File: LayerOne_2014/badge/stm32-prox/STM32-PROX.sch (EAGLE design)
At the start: 167 parts, among them IC10 74XX244-OCTAL-TRISTATE-BUFFERS, IC105 MCP1824T-250, IC106 MCP1824T-120, IC11 CD4066, IC13 PQ1X331M2ZP-3V3-LDO-SOT-23-5, IC14 AD8052, IC2 STM32F103RET6, IC3 PQ1X331M2ZP-3V3-LDO-SOT-23-5, IC4 HCU-INVERTER, IC5 TLV3502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

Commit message: 
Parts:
- added R7, R8: 27, resistor:R-US_R0805
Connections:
- new net N$1: IC2.PA11/UART1CTS/CNRX/TIM1CH4/USBD-, R7.2
- new net N$7: IC2.PA12/UART1RTS/CNTX/TIM1ETR/USBD+, R8.2
- net USB_D+: now also R8.1; no longer IC2.PA12/UART1RTS/CNTX/TIM1ETR/USBD+
- net USB_D-: now also R7.1; no longer IC2.PA11/UART1CTS/CNRX/TIM1CH4/USBD-
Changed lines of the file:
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@@
 <grid distance="0.1" unitdist="inch" unit="inch" style="lines" multiple="1" display="no" altdistance="0.01" altunitdist="inch" altunit="inch"/>
 <layers>
-<layer number="1" name="Top" color="4" fill="1" visible="yes" active="no"/>
-<layer number="2" name="Route2" color="1" fill="3" visible="yes" active="no"/>
-<layer number="3" name="Route3" color="4" fill="3" visible="yes" active="no"/>
-<layer number="4" name="Route4" color="1" fill="4" visible="yes" active="no"/>
-<layer number="5" name="Route5" color="4" fill="4" visible="yes" active="no"/>
-<layer number="6" name="Route6" color="1" fill="8" visible="yes" active="no"/>
-<layer number="7" name="Route7" color="4" fill="8" visible="yes" active="no"/>
-<layer number="8" name="Route8" color="1" fill="2" visible="yes" active="no"/>
-<layer number="9" name="Route9" color="4" fill="2" visible="yes" active="no"/>
-<layer number="10" name="Route10" color="1" fill="7" visible="yes" active="no"/>
-<layer number="11" name="Route11" color="4" fill="7" visible="yes" active="no"/>
-<layer number="12" name="Route12" color="1" fill="5" visible="yes" active="no"/>
-<layer number="13" name="Route13" color="4" fill="5" visible="yes" active="no"/>
-<layer number="14" name="Route14" color="1" fill="6" visible="yes" active="no"/>
-<layer number="15" name="Route15" color="4" fill="6" visible="yes" active="no"/>
-<layer number="16" name="Bottom" color="1" fill="1" visible="yes" active="no"/>
-<layer number="17" name="Pads" color="2" fill="1" visible="yes" active="no"/>
-<layer number="18" name="Vias" color="2" fill="1" visible="yes" active="no"/>
-<layer number="19" name="Unrouted" color="6" fill="1" visible="yes" active="no"/>
-<layer number="20" name="Dimension" color="15" fill="1" visible="yes" active="no"/>
-<layer number="21" name="tPlace" color="7" fill="1" visible="yes" active="no"/>
-<layer number="22" name="bPlace" color="7" fill="1" visible="yes" active="no"/>
-<layer number="23" name="tOrigins" color="15" fill="1" visible="yes" active="no"/>
-<layer number="24" name="bOrigins" color="15" fill="1" visible="yes" active="no"/>
-<layer number="25" name="tNames" color="7" fill="1" visible="yes" active="no"/>
-<layer number="26" name="bNames" color="7" fill="1" visible="yes" active="no"/>
-<layer number="27" name="tValues" color="7" fill="1" visible="yes" active="no"/>
-<layer number="28" name="bValues" color="7" fill="1" visible="yes" active="no"/>
+<layer number="1" name="Top" color="4" fill="1" visible="no" active="no"/>
+<layer number="2" name="Route2" color="1" fill="3" visible="no" active="no"/>
+<layer number="3" name="Route3" color="4" fill="3" visible="no" active="no"/>
+<layer number="4" name="Route4" color="1" fill="4" visible="no" active="no"/>
+<layer number="5" name="Route5" color="4" fill="4" visible="no" active="no"/>
+<layer number="6" name="Route6" color="1" fill="8" visible="no" active="no"/>
+<layer number="7" name="Route7" color="4" fill="8" visible="no" active="no"/>
+<layer number="8" name="Route8" color="1" fill="2" visible="no" active="no"/>
+<layer number="9" name="Route9" color="4" fill="2" visible="no" active="no"/>
+<layer number="10" name="Route10" color="1" fill="7" visible="no" active="no"/>
+<layer number="11" name="Route11" color="4" fill="7" visible="no" active="no"/>
+<layer number="12" name="Route12" color="1" fill="5" visible="no" active="no"/>
+<layer number="13" name="Route13" color="4" fill="5" visible="no" active="no"/>
+<layer number="14" name="Route14" color="1" fill="6" visible="no" active="no"/>
+<layer number="15" name="Route15" color="4" fill="6" visible="no" active="no"/>
+<layer number="16" name="Bottom" color="1" fill="1" visible="no" active="no"/>
+<layer number="17" name="Pads" color="2" fill="1" visible="no" active="no"/>
+<layer number="18" name="Vias" color="2" fill="1" visible="no" active="no"/>
+<layer number="19" name="Unrouted" color="6" fill="1" visible="no" active="no"/>
+<layer number="20" name="Dimension" color="15" fill="1" visible="no" active="no"/>
+<layer number="21" name="tPlace" color="7" fill="1" visible="no" active="no"/>
+<layer number="22" name="bPlace" color="7" fill="1" visible="no" active="no"/>
+<layer number="23" name="tOrigins" color="15" fill="1" visible="no" active="no"/>
+<layer number="24" name="bOrigins" color="15" fill="1" visible="no" active="no"/>
+<layer number="25" name="tNames" color="7" fill="1" visible="no" active="no"/>
+<layer number="26" name="bNames" color="7" fill="1" visible="no" active="no"/>
+<layer number="27" name="tValues" color="7" fill="1" visible="no" active="no"/>
+<layer number="28" name="bValues" color="7" fill="1" visible="no" active="no"/>
 <layer number="29" name="tStop" color="7" fill="3" visible="no" active="no"/>
 <layer number="30" name="bStop" color="7" fill="6" visible="no" active="no"/>
@@
 <layer number="35" name="tGlue" color="7" fill="4" visible="no" active="no"/>
 <layer number="36" name="bGlue" color="7" fill="5" visible="no" active="no"/>
-<layer number="37" name="tTest" color="7" fill="1" visible="yes" active="no"/>
-<layer number="38" name="bTest" color="7" fill="1" visible="yes" active="no"/>
+<layer number="37" name="tTest" color="7" fill="1" visible="no" active="no"/>
+<layer number="38" name="bTest" color="7" fill="1" visible="no" active="no"/>
 <layer number="39" name="tKeepout" color="4" fill="11" visible="no" active="no"/>
 <layer number="40" name="bKeepout" color="1" fill="11" visible="no" active="no"/>
@@
 <layer number="44" name="Drills" color="7" fill="1" visible="no" active="no"/>
 <layer number="45" name="Holes" color="7" fill="1" visible="no" active="no"/>
-<layer number="46" name="Milling" color="3" fill="1" visible="yes" active="no"/>
-<layer number="47" name="Measures" color="7" fill="1" visible="yes" active="no"/>
-<layer number="48" name="Document" color="7" fill="1" visible="yes" active="no"/>
-<layer number="49" name="Reference" color="7" fill="1" visible="yes" active="no"/>
-<layer number="50" name="dxf" color="7" fill="1" visible="yes" active="no"/>
-<layer number="51" name="tDocu" color="7" fill="1" visible="yes" active="no"/>
-<layer number="52" name="bDocu" color="7" fill="1" visible="yes" active="no"/>
-<layer number="53" name="tGND_GNDA" color="7" fill="1" visible="yes" active="no"/>
-<layer number="54" name="bGND_GNDA" color="7" fill="1" visible="yes" active="no"/>
-<layer number="56" name="wert" color="7" fill="1" visible="yes" active="no"/>
+<layer number="46" name="Milling" color="3" fill="1" visible="no" active="no"/>
+<layer number="47" name="Measures" color="7" fill="1" visible="no" active="no"/>
+<layer number="48" name="Document" color="7" fill="1" visible="no" active="no"/>
+<layer number="49" name="Reference" color="7" fill="1" visible="no" active="no"/>
+<layer number="50" name="dxf" color="7" fill="1" visible="no" active="no"/>
+<layer number="51" name="tDocu" color="7" fill="1" visible="no" active="no"/>
+<layer number="52" name="bDocu" color="7" fill="1" visible="no" active="no"/>
+<layer number="53" name="tGND_GNDA" color="7" fill="1" visible="no" active="no"/>
+<layer number="54" name="bGND_GNDA" color="7" fill="1" visible="no" active="no"/>
+<layer number="56" name="wert" color="7" fill="1" visible="no" active="no"/>
 <layer number="91" name="Nets" color="2" fill="1" visible="yes" active="yes"/>
 <layer number="92" name="Busses" color="1" fill="1" visible="yes" active="yes"/>
@@
 <part name="VDD12" library="supply1" deviceset="VDD" device=""/>
 <part name="IC105" library="proxmark" deviceset="TPS799*" device="" technology="25" value="MCP1824T-250"/>
+<part name="R7" library="resistor" deviceset="R-US_" device="R0805" value="27">
+<attribute name="PARTNO" value="*"/>
+</part>
+<part name="R8" library="resistor" deviceset="R-US_" device="R0805" value="27">
+<attribute name="PARTNO" value="*"/>
+</part>
 </parts>
 <sheets>
@@
 <attribute name="NAME" x="6.35" y="25.146" size="1.778" layer="95"/>
 <attribute name="VALUE" x="4.826" y="18.796" size="1.778" layer="96"/>
+</instance>
+<instance part="R7" gate="G$1" x="58.42" y="-12.7">
+<attribute name="PARTNO" x="58.42" y="-12.7" size="1.778" layer="96" display="off"/>
+</instance>
+<instance part="R8" gate="G$1" x="71.12" y="-12.7" rot="R180">
+<attribute name="PARTNO" x="71.12" y="-12.7" size="1.778" layer="96" rot="R180" display="off"/>
 </instance>
 </instances>
@@
 <net name="USB_D-" class="0">
 <segment>
+<wire x1="53.34" y1="-12.7" x2="50.8" y2="-12.7" width="0.1524" layer="91"/>
+<label x="50.8" y="-12.7" size="1.778" layer="95" rot="R180"/>
+<pinref part="R7" gate="G$1" pin="1"/>
+</segment>
+</net>
+<net name="USB_D+" class="0">
+<segment>
+<wire x1="76.2" y1="-12.7" x2="78.74" y2="-12.7" width="0.1524" layer="91"/>
+<pinref part="R8" gate="G$1" pin="1"/>
+<label x="78.74" y="-12.7" size="1.778" layer="95"/>
+</segment>
+</net>
+<net name="N$1" class="0">
+<segment>
 <pinref part="IC2" gate="G$1" pin="PA11/UART1CTS/CNRX/TIM1CH4/USBD-"/>
-<wire x1="63.5" y1="0" x2="63.5" y2="-10.16" width="0.1524" layer="91"/>
-<label x="60.96" y="-10.16" size="1.778" layer="95" rot="R270"/>
-</segment>
-</net>
-<net name="USB_D+" class="0">
+<pinref part="R7" gate="G$1" pin="2"/>
+<wire x1="63.5" y1="-12.7" x2="63.5" y2="0" width="0.1524" layer="91"/>
+</segment>
+</net>
+<net name="N$7" class="0">
 <segment>
 <pinref part="IC2" gate="G$1" pin="PA12/UART1RTS/CNTX/TIM1ETR/USBD+"/>
-<wire x1="66.04" y1="0" x2="66.04" y2="-10.16" width="0.1524" layer="91"/>
-<label x="63.5" y="-10.16" size="1.778" layer="95" rot="R270"/>
-</segment>
-</net>
+<pinref part="R8" gate="G$1" pin="2"/>
+<wire x1="66.04" y1="-12.7" x2="66.04" y2="0" width="0.1524" layer="91"/>
+</segment>
+</net>

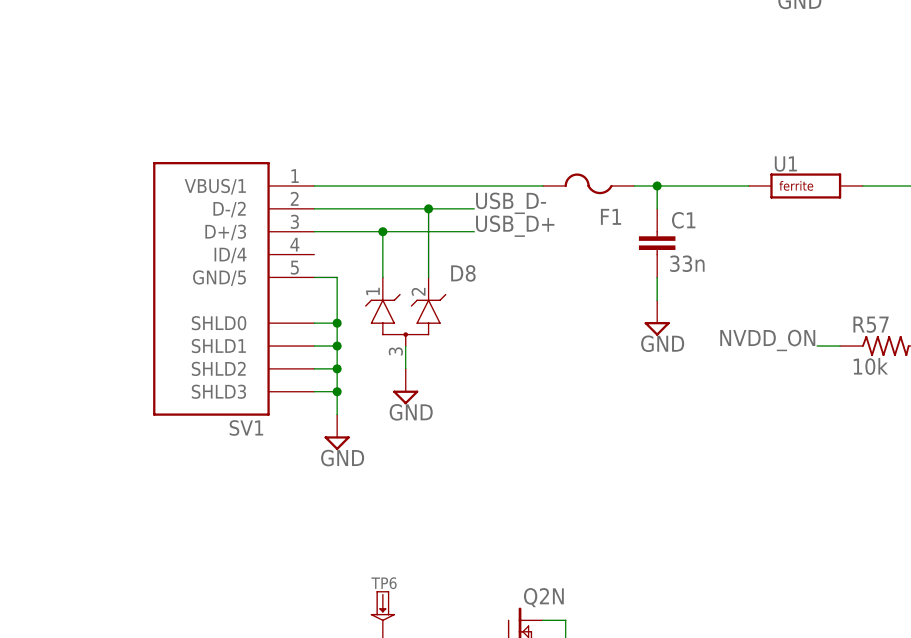
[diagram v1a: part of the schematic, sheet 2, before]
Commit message: changed 10uF CPOL electrolytics to tants D/7343-31R
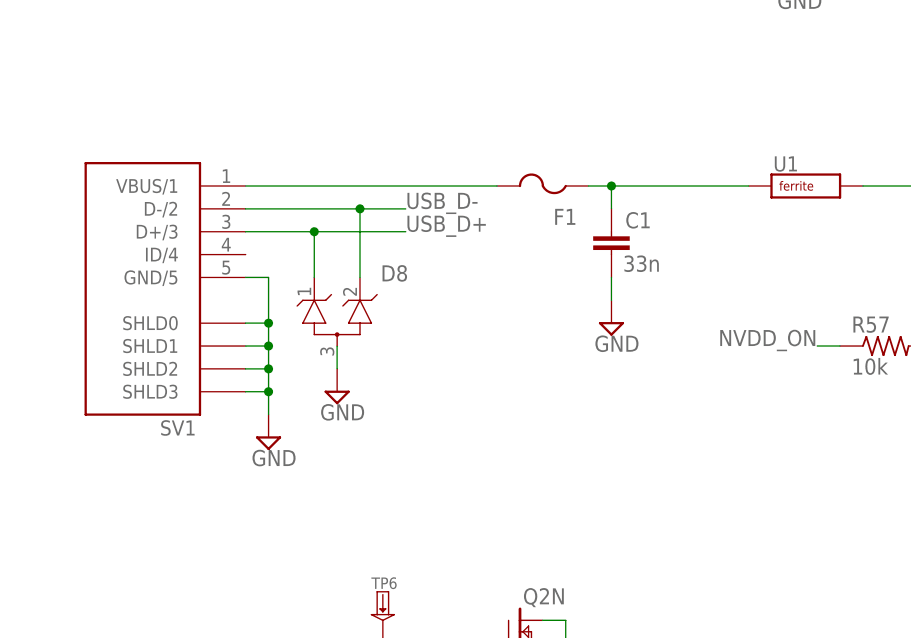
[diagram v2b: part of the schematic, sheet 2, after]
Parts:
- C37, C38: device merged:CAPACITOR-POLARIZEDALCHIP-MZA-F80 -> adafruit:CPOL-USD/7343-31R
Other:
- note added: "l1 isn't needed"
- moved on the sheet: C1, D8, F1, SV1

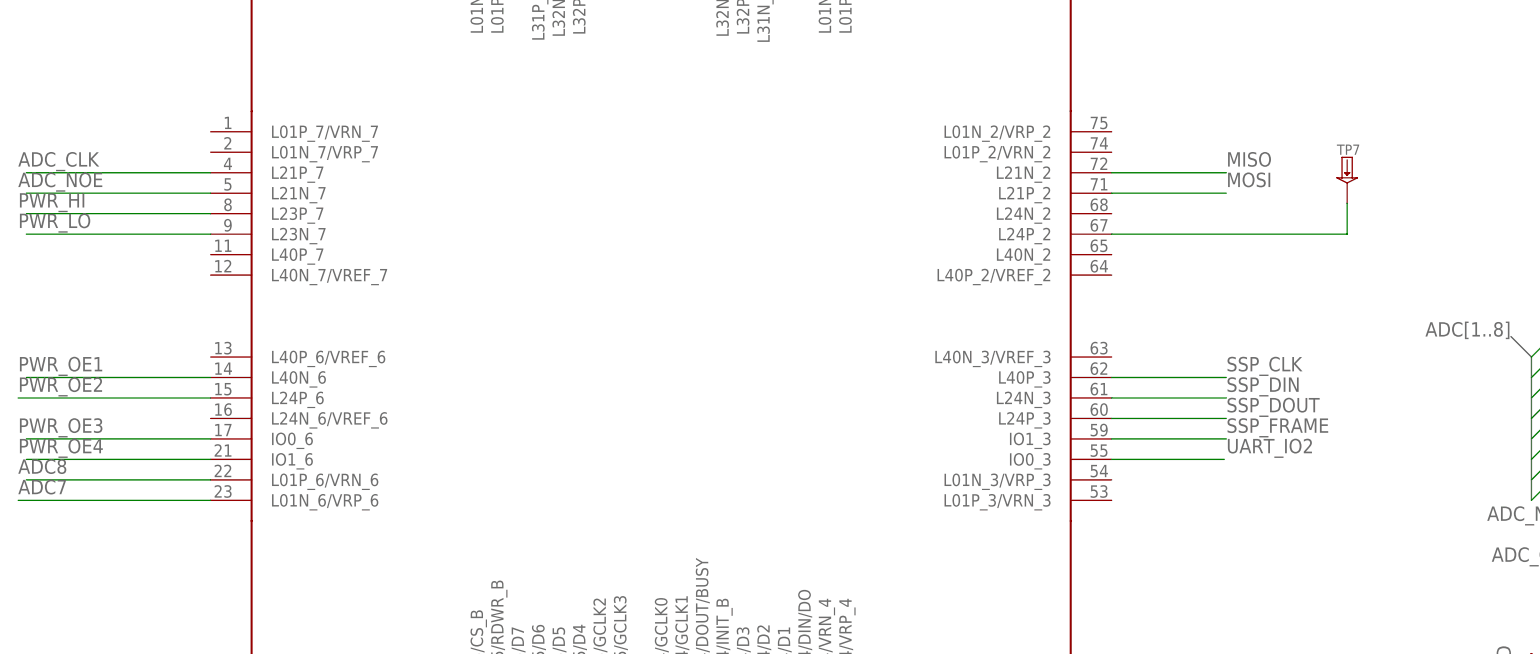
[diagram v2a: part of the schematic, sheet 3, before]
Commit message: Update pins such that left/right were swapped to make layout easy
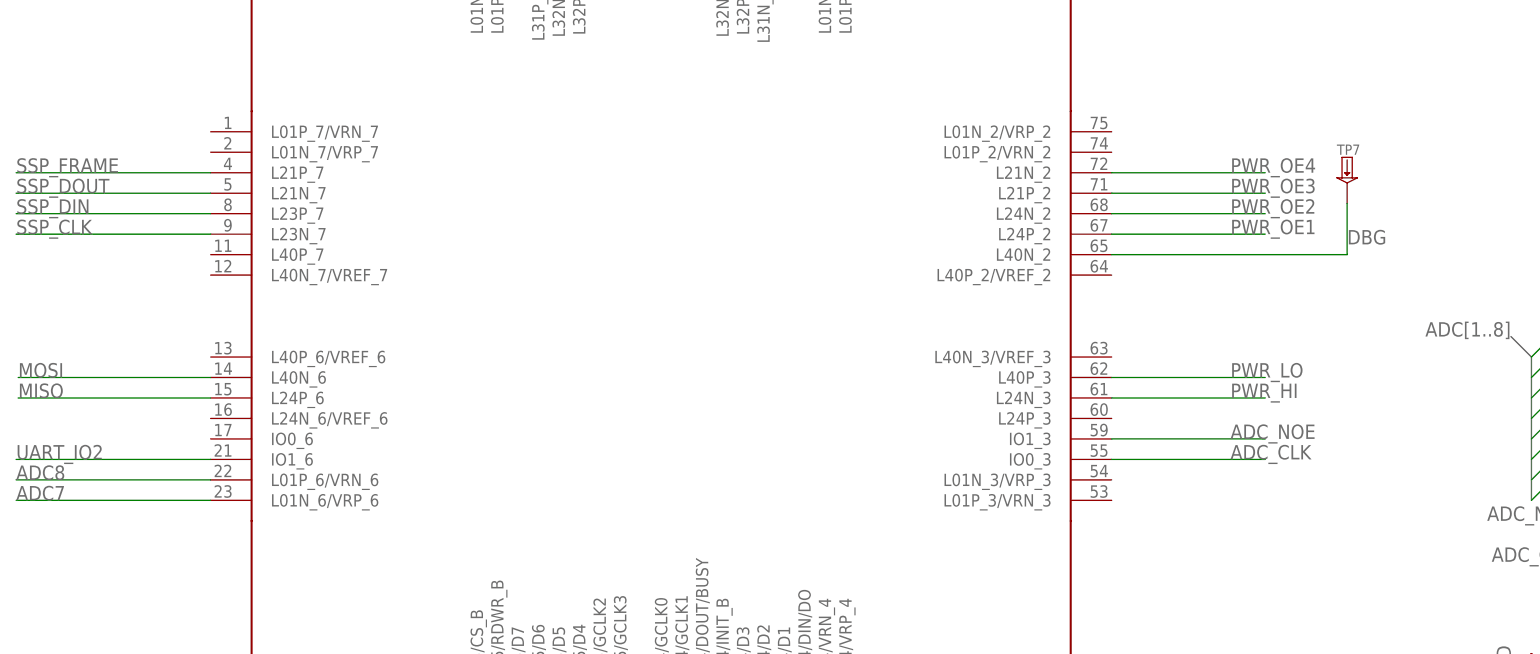
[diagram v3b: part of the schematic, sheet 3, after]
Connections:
- removed net N$55: TP7.P$1, U2G$1.L24P_2
- new net DBG: TP7.P$1, U2G$1.L40N_2
- net ADC_CLK: now also U2G$1.IO0_3; no longer U2G$1.L21P_7
- net ADC_NOE: now also U2G$1.IO1_3; no longer U2G$1.L21N_7
- net MISO: now also U2G$1.L24P_6; no longer U2G$1.L21N_2
- net MOSI: now also U2G$1.L40N_6; no longer U2G$1.L21P_2
- net PWR_HI: now also U2G$1.L24N_3; no longer U2G$1.L23P_7
- net PWR_LO: now also U2G$1.L40P_3; no longer U2G$1.L23N_7
- net PWR_OE1: now also U2G$1.L24P_2; no longer U2G$1.L40N_6
- net PWR_OE2: now also U2G$1.L24N_2; no longer U2G$1.L24P_6
- net PWR_OE3: now also U2G$1.L21P_2; no longer U2G$1.IO0_6
- net PWR_OE4: now also U2G$1.L21N_2; no longer U2G$1.IO1_6
- net SSP_CLK: now also U2G$1.L23N_7; no longer U2G$1.L40P_3
- net SSP_DIN: now also U2G$1.L23P_7; no longer U2G$1.L24N_3
- net SSP_DOUT: now also U2G$1.L21N_7; no longer U2G$1.L24P_3
- net SSP_FRAME: now also U2G$1.L21P_7; no longer U2G$1.IO1_3
- net UART_IO2: now also U2G$1.IO1_6; no longer U2G$1.IO0_3

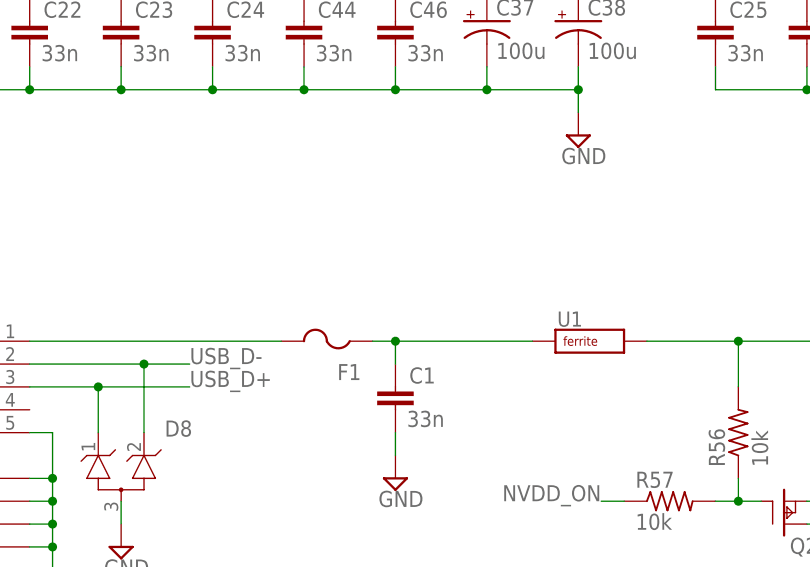
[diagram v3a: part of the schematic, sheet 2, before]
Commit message: 
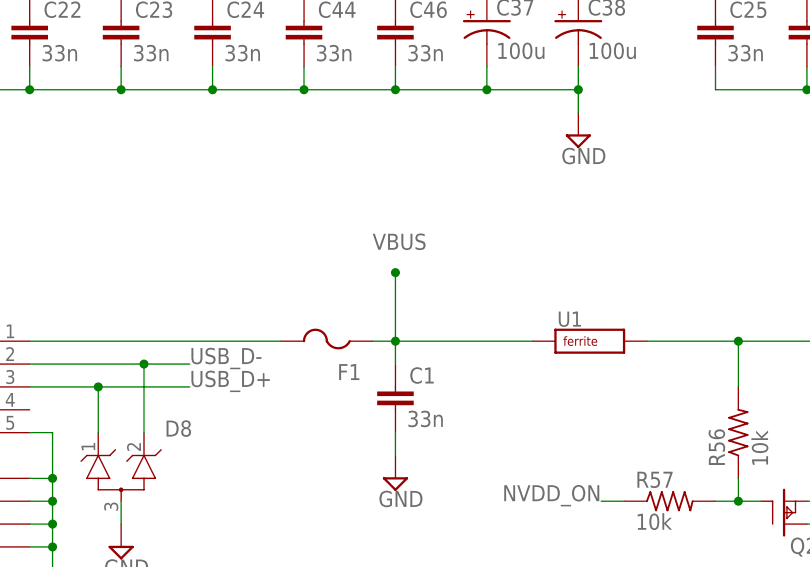
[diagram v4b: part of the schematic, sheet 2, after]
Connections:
- net N$6 renamed VBUS
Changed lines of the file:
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@@
 <setting verticaltext="up"/>
 </settings>
-<grid distance="0.1" unitdist="inch" unit="inch" style="lines" multiple="1" display="yes" altdistance="0.01" altunitdist="inch" altunit="inch"/>
+<grid distance="0.1" unitdist="inch" unit="inch" style="lines" multiple="1" display="no" altdistance="0.01" altunitdist="inch" altunit="inch"/>
 <layers>
 <layer number="1" name="Top" color="4" fill="1" visible="no" active="no"/>
@@
 </segment>
 </net>
-<net name="N$6" class="0">
+<net name="VBUS" class="0">
 <segment>
 <wire x1="22.86" y1="58.42" x2="38.1" y2="58.42" width="0.1524" layer="91"/>
@@
 <wire x1="22.86" y1="58.42" x2="20.32" y2="58.42" width="0.1524" layer="91"/>
 <junction x="22.86" y="58.42"/>
-</segment>
-</net>
+<wire x1="22.86" y1="58.42" x2="22.86" y2="66.04" width="0.1524" layer="91"/>
+<junction x="22.86" y="66.04"/>
+<label x="20.32" y="68.58" size="1.778" layer="95"/>
+</segment>
+</net>

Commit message: 
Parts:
- added C57, C58, C59, C60, C61: (no value), badge.lbrbadge_2013:SPARKFUN_CAP0603-CAP
- added C62: 10uH, badge.lbrbadge_2013:SPARKFUN_CAP0603-CAP
- added C63: .1uF, badge.lbrbadge_2013:SPARKFUN_CAP0603-CAP
- added C64: 10uF, badge.lbrbadge_2013:SPARKFUN_CAP0603-CAP
- added IC1: IC_TPS6120X-QFN10, dp_devices:IC_TPS6120X-QFN10
- added L2: CDRH2D18/HPNP-2R2NC, pwr_section:CDRH2D18
- added LED1, LED2: (no value), badge.lbrbadge_2013:LED_LEDCHIP-LED0603
- added R24, R25, R26, R43: (no value), badge.lbrbadge_2013:RCL_R-US_R0603
- added R55: 1650K 1%, badge.lbrbadge_2013:RCL_R-US_R0603
- added R60: 150K 1%, badge.lbrbadge_2013:RCL_R-US_R0603
- added TP10, TP8, TP9: --MERGED_TESTPADKEYSTONE-SMD, STM32-PROX:--MERGED_TESTPADKEYSTONE-SMD
- added U$7: MC34674, STM32-PROX:MC34674
- added U$9: BATT, STM32-PROX:BATT
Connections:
- new net 5V: C64.1, IC1IC.FB, IC1IC.VOUT, TP10.P$1, U1.A
- new net N$55: C58.1, LED1.C, R25.1
- new net N$6: C57.1, LED2.C, R24.1
- new net N$63: R25.2, U$7.!RED
- new net N$64: R26.1, U$7.VREF
- new net N$65: C60.1, R26.2, R43.2, U$7.TEMP
- new net N$66: C63.1, IC1IC.VAUX
- new net N$67: IC1IC.UVLO, R55.1, R60.2
- new net N$68: IC1IC.L, L2.2
- new net N$8: R24.2, U$7.!GRN
- new net NTC: R43.1, U$9.NTC
- new net ONOFF: IC1IC.EN
- new net PGND: C63.2, C64.2, IC1IC.GND, IC1IC.PGND
- new net VBAT+: C61.1, C62.1, IC1IC.PS, IC1IC.VIN, L2.1, R55.2, TP9.P$1, U$7.BAT, U$9.POS
- new net VBAT-: C61.2, U$9.NEG
- net GND: now also C57.2, C58.2, C59.2, C60.2, C62.2, R60.1, U$7.!EN, U$7.EP, U$7.GND
- net VBUS: now also C59.1, LED1.A, LED2.A, TP8.P$1, U$7.VIN; no longer U1.A

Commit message: 
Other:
- note added: "Sheet 1"
